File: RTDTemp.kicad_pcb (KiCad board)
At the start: 2 copper layers, 92 parts, among them J11 Conn_01x02, J4 CAN_In, J5 CAN_Out, U2 Nucleo_L432KC, U3 PDS1-Sx-Sx, U5 ADM3055E, U7 CDSOT23-T24CAN

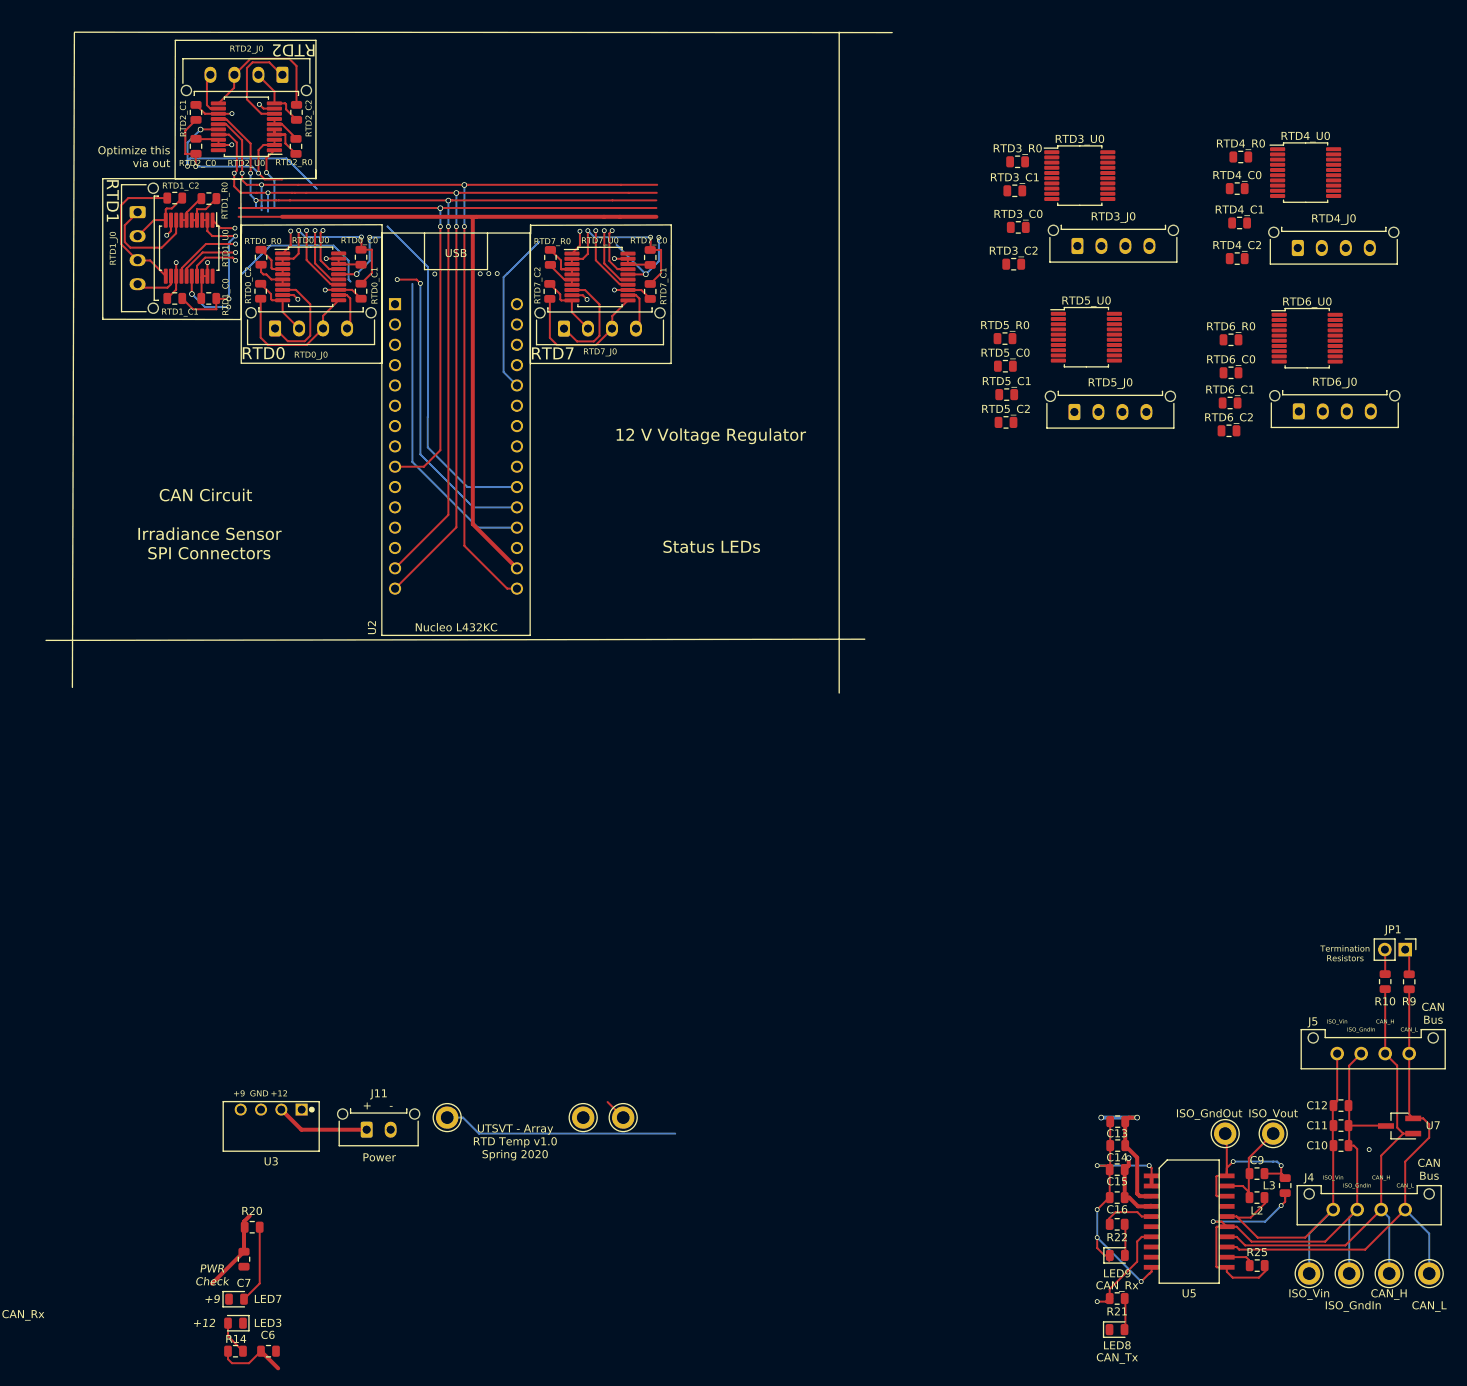
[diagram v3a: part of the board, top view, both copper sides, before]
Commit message: Arragned Board
Arragned Board, room for optimization
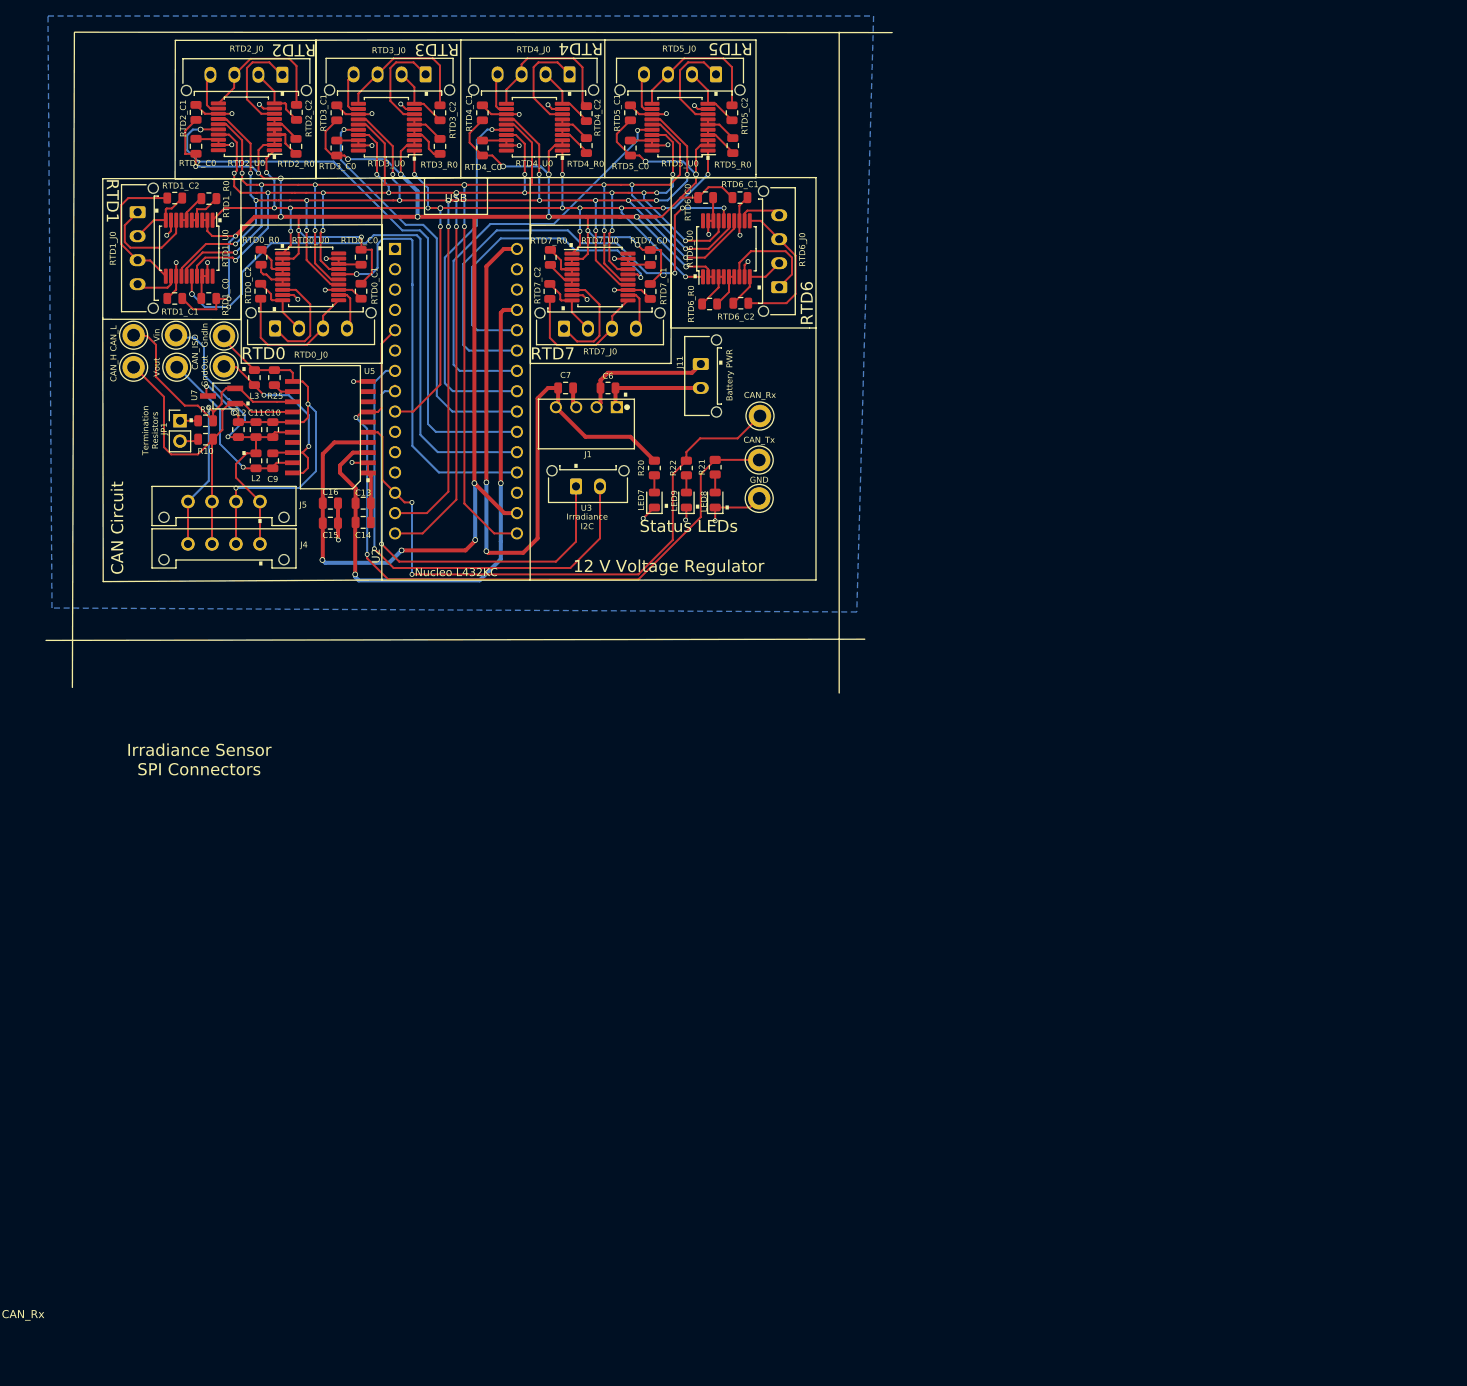
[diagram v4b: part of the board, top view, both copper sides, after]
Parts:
- removed LED3: Car Power Live?, LED_SMD:LED_0805_2012Metric
- removed R14: 2K, Resistor_SMD:R_0805_2012Metric
- removed TP19: CAN_Tx, TestPoint:TestPoint_Keystone_5005-5009_Compact
- removed TP20: CAN_Rx, TestPoint:TestPoint_Keystone_5005-5009_Compact
- removed TP26: GND, TestPoint:TestPoint_Keystone_5005-5009_Compact
- added CAN_Rx: CAN_Rx, TestPoint:TestPoint_Keystone_5005-5009_Compact, F.Cu at (179.6, 67.4)
- added CAN_Tx: CAN_Tx, TestPoint:TestPoint_Keystone_5005-5009_Compact, F.Cu at (179.4, 72.9)
- added GND: GND, TestPoint:TestPoint_Keystone_5005-5009_Compact, F.Cu at (179.4, 77.7)
- added J1: Conn_01x02, Connector_Molex:Molex_Micro-Fit_3.0_43650-0215_1x02_P3.00mm_Vertical, F.Cu at (156.6, 76.2)
- moved TP22 200.0 mm to (101.2, 57.3)
- moved TP21 193.6 mm to (101.2, 61.3)
- moved TP14 183.9 mm to (106.5, 57.3)
- moved TP15 183.1 mm to (112.5, 57.4)
- moved U7 173.2 mm to (112.2, 64.9)
- moved TP13 167.2 mm to (106.7, 61.3)
- moved JP1 166.8 mm to (107.0, 68.0), turned to 0 degrees
- moved R9 166.0 mm to (110.2, 68.0), turned to 0 degrees
- moved R25 165.6 mm to (118.8, 62.6), turned to 90 degrees
- moved L3 163.7 mm to (116.3, 62.6), turned to 270 degrees
- moved R10 162.3 mm to (110.2, 70.3), turned to 0 degrees
- moved C12 161.7 mm to (114.3, 69.1), turned to 90 degrees
- moved C11 161.1 mm to (116.5, 69.1), turned to 90 degrees
- moved C10 160.7 mm to (118.7, 69.1), turned to 90 degrees
- moved J4 157.9 mm to (117.0, 83.4), turned to 180 degrees
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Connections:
- J11 pad 2: GND -> GNDPWR
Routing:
- net +3V3: track 198.0 -> 340.1 mm, vias 9 -> 24
- net +9VA: track 10.6 -> 86.3 mm, vias 0 -> 2
- net /CAN_Rx: track 9.55 -> 79.1 mm, vias 0 -> 2
- net SDI: track 139.3 -> 206.8 mm, vias 7 -> 17
- net CS_6: track 0.00 -> 62.9 mm, vias 0 -> 3
- net Net-(J1-Pad2): track 0.00 -> 61.2 mm, vias 0 -> 1
- net CLK: track 141.6 -> 202.6 mm, vias 7 -> 11
- net SDO: track 140.4 -> 196.2 mm, vias 7 -> 17
- net Net-(J1-Pad1): track 0.00 -> 54.3 mm, vias 0 -> 1
- net +5V: track 17.8 -> 71.4 mm
- net CS_5: track 0.00 -> 53.5 mm, vias 0 -> 1
- net CS_3: track 0.13 -> 52.4 mm, vias 0 -> 1
- net /CAN_Tx: track 42.6 -> 92.7 mm, vias 1 -> 2
- net CS_4: track 0.00 -> 45.7 mm, vias 0 -> 1
- net DRDY: track 106.8 -> 145.9 mm, vias 6 -> 16
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- added copper zone on B.Cu, net GND
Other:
- board text added: "."
- board text added: "Battery PWR"
- board text added: "CAN_ISO"
- board text added: "GndIn"
- board text added: "GndOut"
- board text added: "Irradiance I2C"
- board text added: "RTD3"
- board text added: "RTD4"
- board text added: "RTD5"
- board text added: "RTD6"
- board text added: "Vin"
- board text added: "Vout"
- board text removed: "+"
- board text removed: "+12"
- board text removed: "+9"
- board text removed: "-"
- board text removed: "CAN Bus"
- board text removed: "ISO_GndIn"
- board text removed: "ISO_GndOut"
- board text removed: "ISO_Vin"
- board text removed: "ISO_Vout"
- board text removed: "Optimize this via out"
- board text removed: "PWR Check"
- board text removed: "Power"
- board text removed: "UTSVT - Array RTD Temp v1.0 Spring 2020"

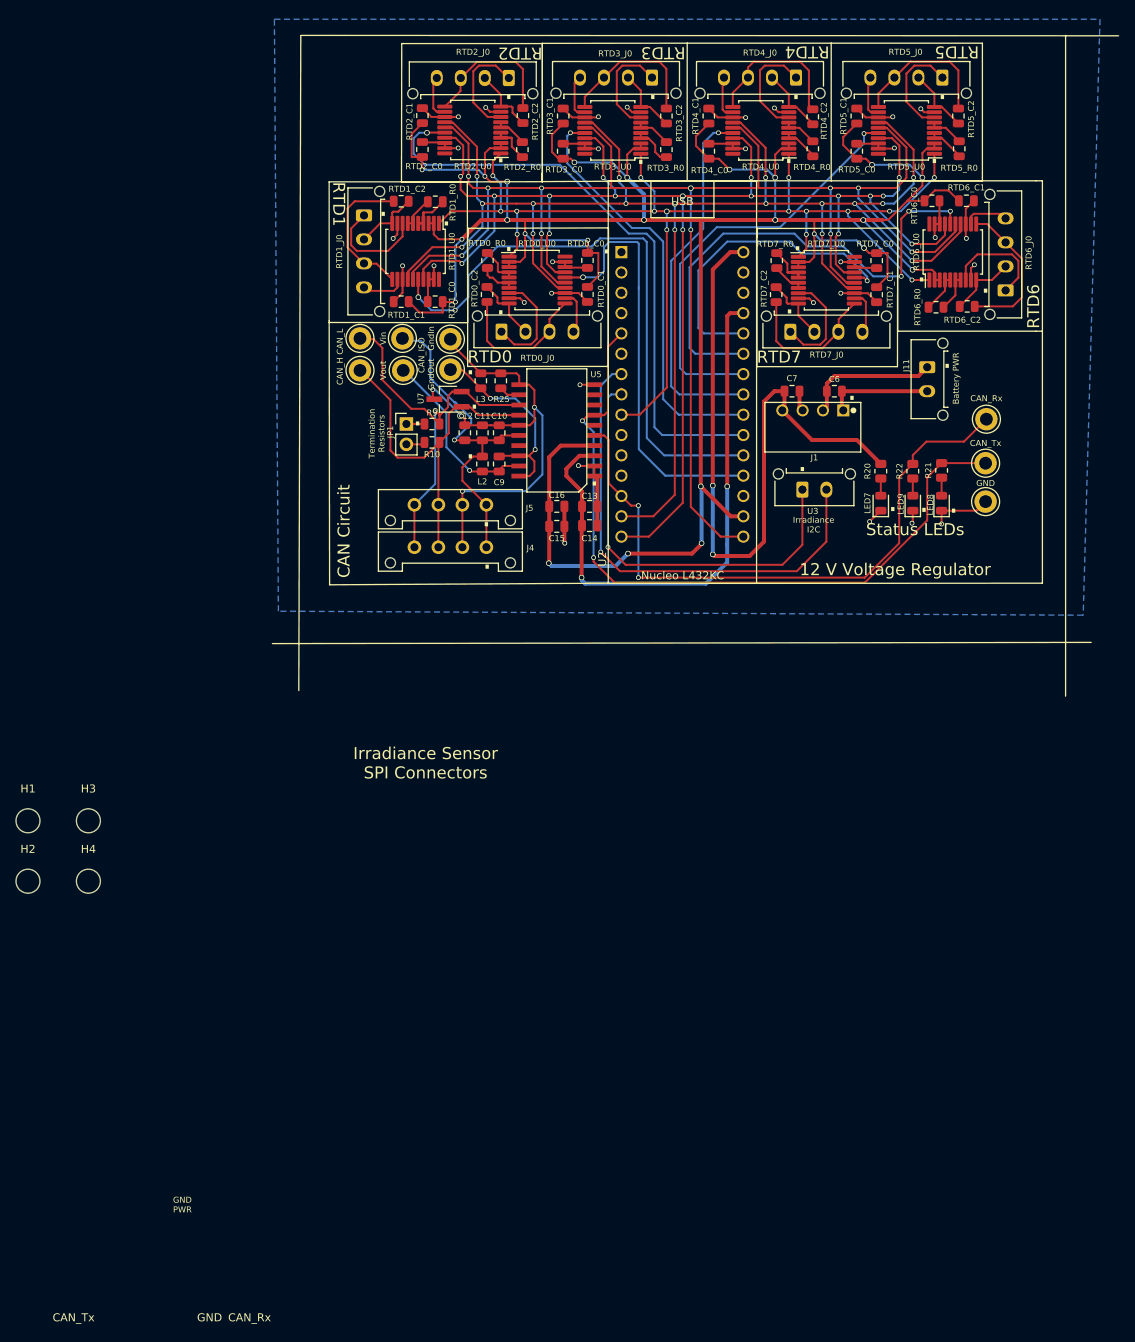
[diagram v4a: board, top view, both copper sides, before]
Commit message: Finished Optimization, Edge cuts, and Placed Drill Holes
Optimized the space as best as I could. Some more space could possibly be saved, or maybe some connections could be made better.
Made the Edge Cuts for the boards. Dimensions right now are 70mm*90mm
Placed Mounting Holes 5mm*5mm away from the corners of the board.
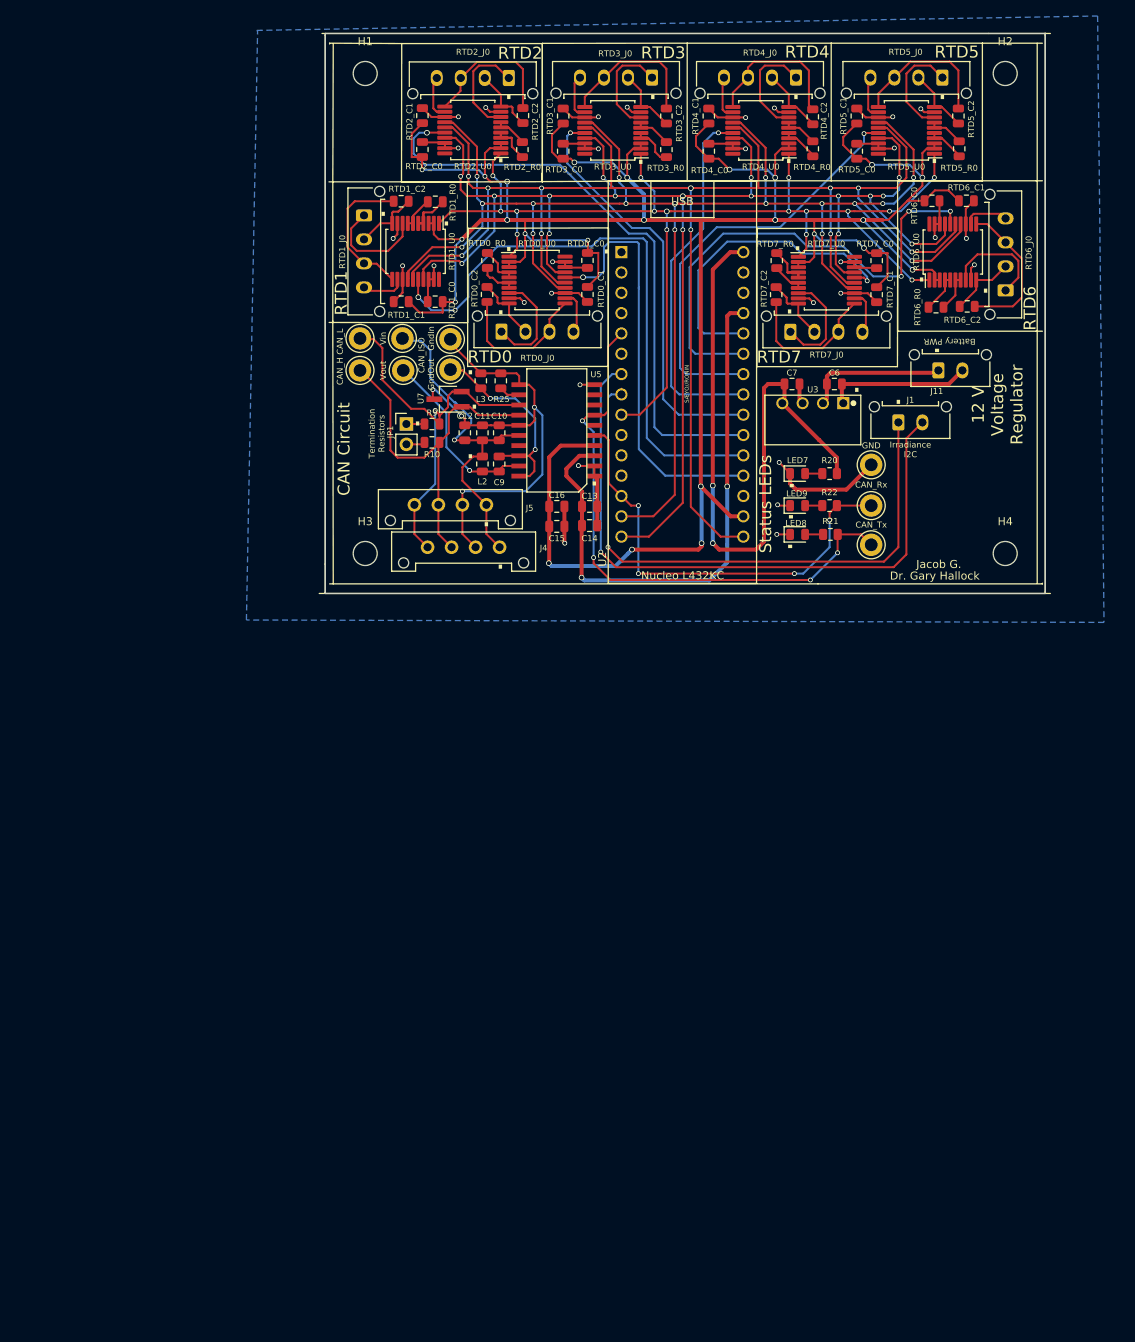
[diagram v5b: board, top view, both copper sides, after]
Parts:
- moved H2 158.5 mm to (181.9, 24.2)
- moved H4 121.7 mm to (181.9, 84.2)
- moved H1 102.5 mm to (101.9, 24.2)
- moved H3 48.1 mm to (101.9, 84.2)
- moved LED8 18.4 mm to (155.9, 81.8), turned to 0 degrees
- moved CAN_Rx 18.0 mm to (165.2, 78.2)
- moved CAN_Tx 17.6 mm to (165.2, 83.1)
- moved R21 16.0 mm to (160.1, 81.8), turned to 0 degrees
- moved GND 15.0 mm to (165.2, 73.1)
- moved J1 14.6 mm to (168.6, 67.8)
- moved LED9 14.4 mm to (155.9, 78.2), turned to 0 degrees
- moved R22 11.3 mm to (159.9, 78.2), turned to 0 degrees
- moved LED7 11.0 mm to (155.9, 74.2), turned to 0 degrees
- moved R20 6.41 mm to (159.9, 74.2), turned to 0 degrees
- moved J4 1.65 mm to (118.7, 83.4)
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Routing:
- net /CAN_Rx: track 79.1 -> 55.9 mm, vias 2 -> 4
- net Net-(J1-Pad1): track 54.3 -> 74.5 mm
- net Net-(J1-Pad2): track 61.2 -> 81.0 mm
- net /CAN_Tx: track 92.7 -> 73.0 mm, vias 2 -> 4
- net GND: track 128.3 -> 134.1 mm
- net GNDPWR: track 13.1 -> 18.0 mm
- net +9VA: track 86.3 -> 81.9 mm
- net Net-(J4-Pad4): track 49.5 -> 50.2 mm
- net Net-(J4-Pad3): track 45.8 -> 46.5 mm
- net Net-(C10-Pad2): track 61.0 -> 61.7 mm
- net Net-(C10-Pad1): track 43.1 -> 43.8 mm
- net +5V: track 71.4 -> 70.9 mm
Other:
- board outline added: 90 x 70 mm
- board text added: "Jacob G."
- board text added: "SÆYO//RONIN"
- board text removed: "CAN_Rx"
- board text removed: "CAN_Tx"
- board text removed: "GND"
- board text removed: "GND PWR"
- board text removed: "Irradiance Sensor SPI Connectors"
